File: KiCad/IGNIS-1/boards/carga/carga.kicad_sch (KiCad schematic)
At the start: 8 parts, among them J1 LiPo_1S, J2 RBF_pin, J40 Backplane, SW1 Main_SW, U2 TPS63020, U40 TP4056

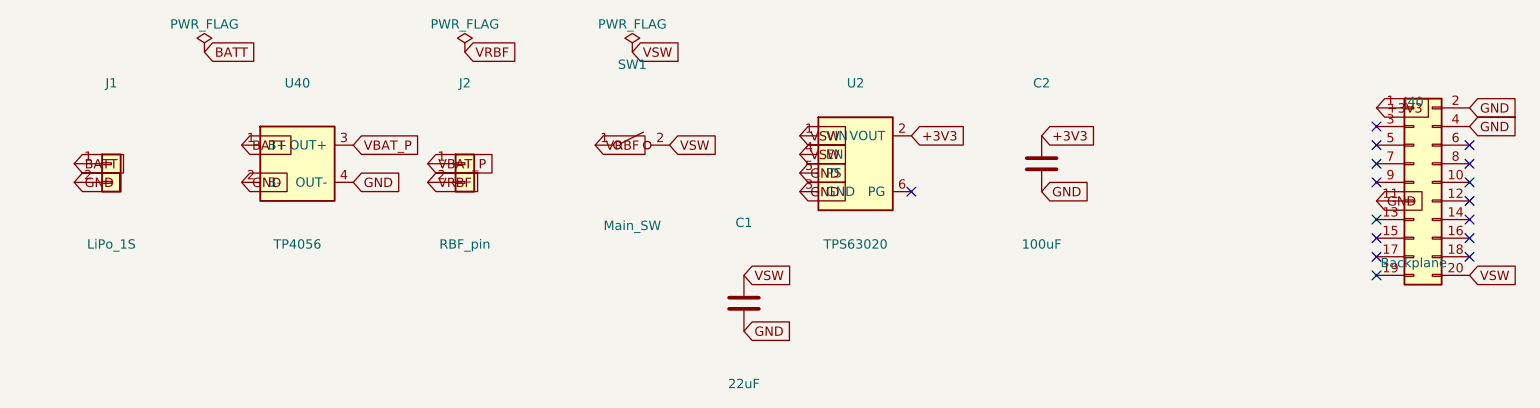
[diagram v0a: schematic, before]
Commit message: 5 boards separados, falta ajustar dimensiones de BME280 y MQ-135
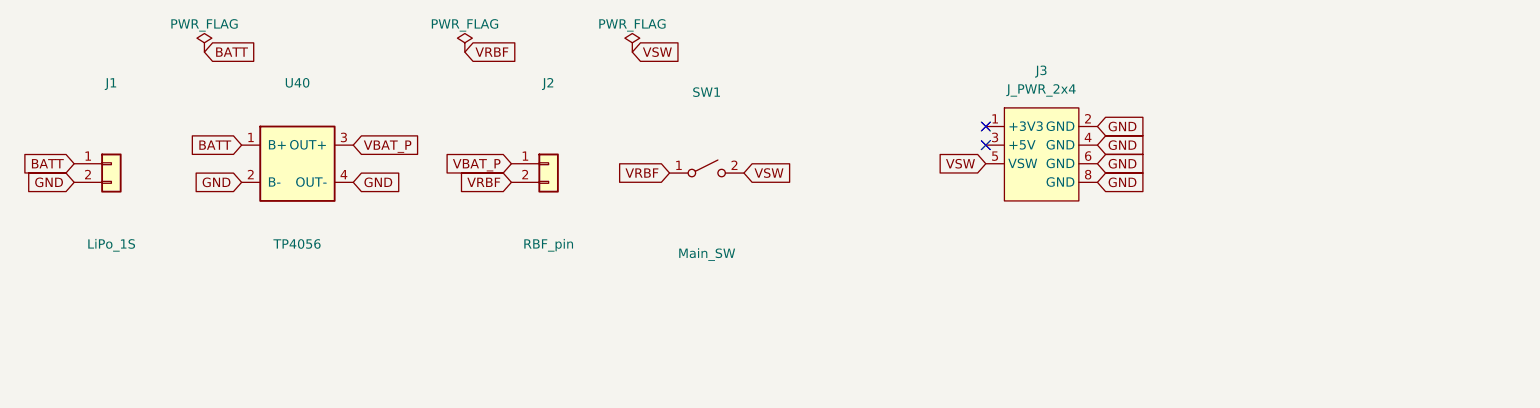
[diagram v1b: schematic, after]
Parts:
- removed C1: 22uF, Capacitor_THT:CP_Radial_D6.3mm_P2.50mm, symbol Device:C
- removed C2: 100uF, Capacitor_THT:CP_Radial_D8.0mm_P3.80mm, symbol Device:C
- removed J40: Backplane, Connector_PinHeader_2.54mm:PinHeader_2x10_P2.54mm_Vertical, symbol Connector_Generic:Conn_02x10_Odd_Even
- removed U2: TPS63020, IGNIS1:TPS63020_module, symbol IGNIS1:TPS63020
- added J3: J_PWR_2x4, IGNIS1:J_PWR_2x4_Keyed, symbol IGNIS1:J_PWR_2x4
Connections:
- net GND: now also J3.2 (GND), J3.4 (GND), J3.6 (GND), J3.8 (GND)
- net VSW: now also J3.5 (VSW)
- no-connect marks 16 -> 2
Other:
- moved on the sheet: J2, SW1
